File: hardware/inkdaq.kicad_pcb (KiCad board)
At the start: 2 copper layers, 6 x 23.2 mm, 3 parts, among them U1 INA333xxDRG

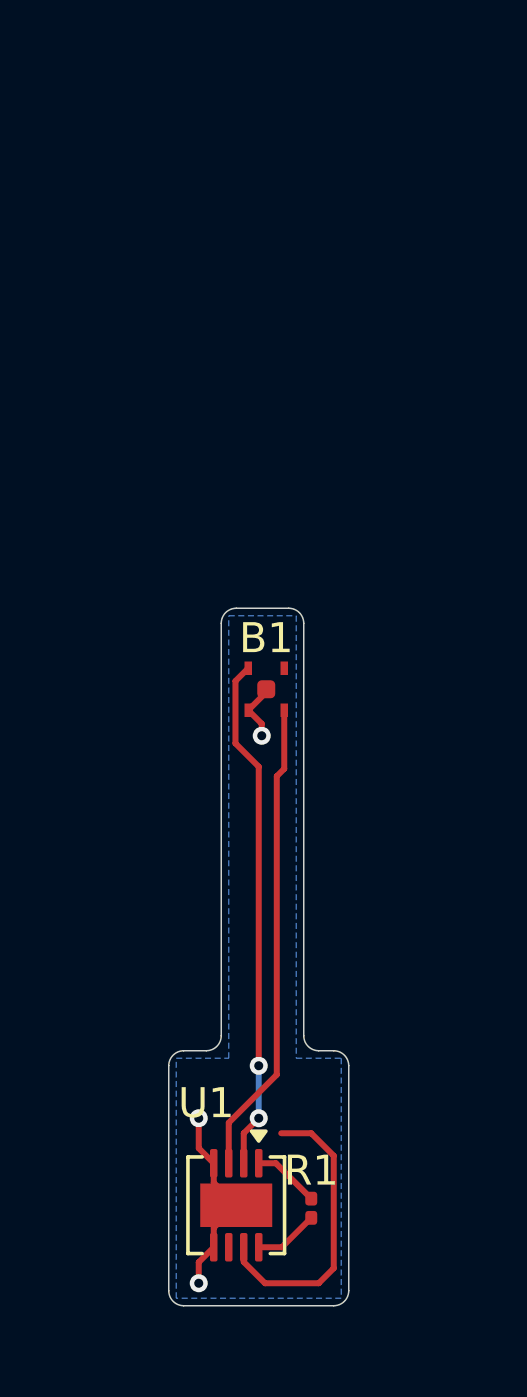
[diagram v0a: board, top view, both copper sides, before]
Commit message: add LCSC part numbers
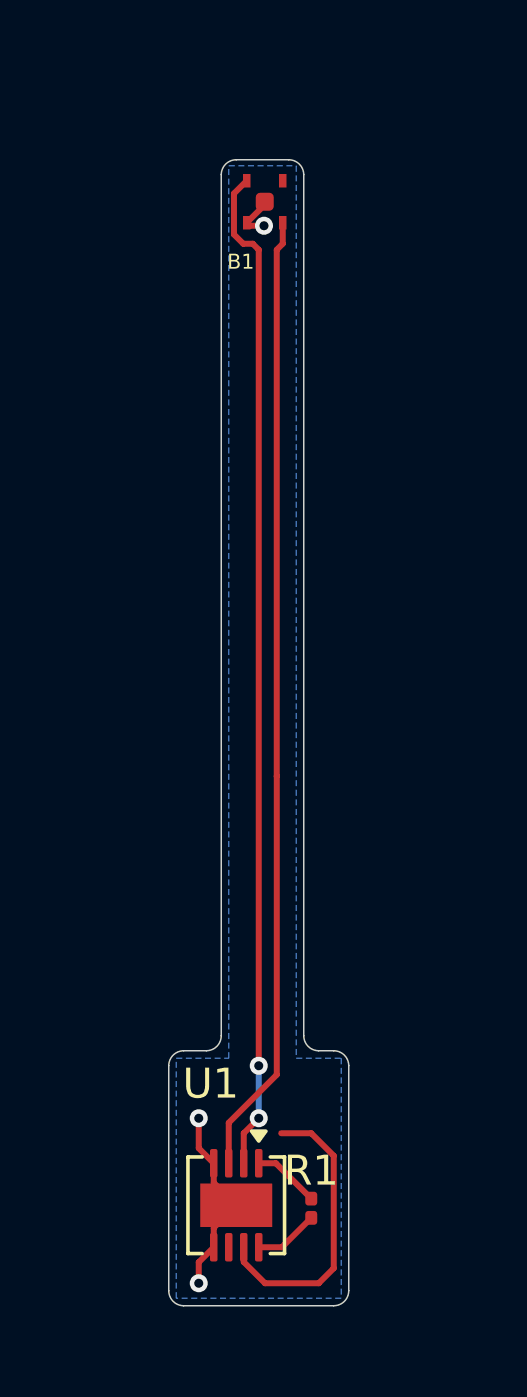
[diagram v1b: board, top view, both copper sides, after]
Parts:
- moved B1 16.3 mm to (157.2, 87.0)
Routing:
- net HSFPAR_V_NEG: track 17.2 -> 33.7 mm
- net HSFPAR_V_POS: track 15.9 -> 32.1 mm
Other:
- board size 6 x 23.2 mm -> 6 x 38.2 mm
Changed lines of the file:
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@@
+			)
+		)
+		(property "LCSC" "C851698"
+			(at 0 0 270)
+			(unlocked yes)
+			(layer "F.Fab")
+			(hide yes)
+			(effects
+				(font
+					(size 1 1)
+					(thickness 0.15)
+				)
 			)
 		)
@@
 	(footprint "inkdaq_footprints:HSFPAR004A"
 		(layer "F.Cu")
-		(at 157.25 103.2)
+		(at 157.2 86.95)
 		(descr "ALPSALPINE HSFPAR Series High-sensitivity Force Sensor")
 		(property "Reference" "B1"
-			(at 0 -4.45 0)
+			(at -0.8 -0.75 0)
 			(unlocked yes)
 			(layer "F.SilkS")
 			(effects
 				(font
-					(size 1 1)
-					(thickness 0.1)
+					(size 0.5 0.5)
+					(thickness 0.05)
 				)
 			)
@@
 		)
 		(property "Description" "ALPSALPINE HSFPAR Series High-sensitivity Force Sensor"
+			(at 0 0 0)
+			(unlocked yes)
+			(layer "F.Fab")
+			(hide yes)
+			(effects
+				(font
+					(size 1 1)
+					(thickness 0.15)
+				)
+			)
+		)
+		(property "LCSC" "C470800"
 			(at 0 0 0)
 			(unlocked yes)
@@
 		(tags "WSON NoLead")
 		(property "Reference" "U1"
-			(at -3.4 1 180)
+			(at -4.05 0.85 180)
 			(layer "F.SilkS")
 			(effects
@@
 				(font
 					(size 1.27 1.27)
+					(thickness 0.15)
+				)
+			)
+		)
+		(property "LCSC" "C2057429"
+			(at 0 0 270)
+			(unlocked yes)
+			(layer "F.Fab")
+			(hide yes)
+			(effects
+				(font
+					(size 1 1)
 					(thickness 0.15)
 				)
@@
 	)
 	(gr_arc
-		(start 158 97.75)
-		(mid 158.353553 97.896447)
-		(end 158.5 98.25)
+		(start 158 82.8)
+		(mid 158.353553 82.946447)
+		(end 158.5 83.3)
 		(stroke
 			(width 0.05)
@@
 	)
 	(gr_line
-		(start 158.5 98.25)
+		(start 158.5 83.3)
 		(end 158.5 112)
 		(stroke
@@
 	(gr_line
 		(start 155.75 112)
-		(end 155.75 98.25)
+		(end 155.75 83.3)
 		(stroke
 			(width 0.05)
@@
 	)
 	(gr_arc
-		(start 155.75 98.25)
-		(mid 155.896447 97.896447)
-		(end 156.25 97.75)
+		(start 155.75 83.3)
+		(mid 155.896447 82.946447)
+		(end 156.25 82.8)
 		(stroke
 			(width 0.05)
@@
 	)
 	(gr_line
-		(start 156.25 97.75)
-		(end 158 97.75)
+		(start 156.25 82.8)
+		(end 158 82.8)
 		(stroke
 			(width 0.05)
@@
 	)
 	(segment
+		(start 156.7 85)
+		(end 156.6 84.9)
+		(width 0.2)
+		(layer "F.Cu")
+		(net 3)
+	)
+	(segment
 		(start 155.5 119.05)
 		(end 155.5 118.4)
@@
 	)
 	(segment
-		(start 157.25 100.45)
-		(end 157.25 100.55)
+		(start 157.2 84.2)
+		(end 157.2 84.3)
 		(width 0.2)
 		(layer "F.Cu")
@@
 	)
 	(segment
-		(start 157.25 100.55)
-		(end 156.65 101.15)
+		(start 157.174998 85)
+		(end 156.7 85)
+		(width 0.2)
+		(layer "F.Cu")
+		(net 3)
+	)
+	(segment
+		(start 157.2 84.3)
+		(end 156.6 84.9)
 		(width 0.2)
 		(layer "F.Cu")
@@
 	)
 	(segment
-		(start 157.1 102)
-		(end 157.1 101.6)
-		(width 0.2)
-		(layer "F.Cu")
-		(net 3)
-	)
-	(segment
 		(start 155 115.75)
 		(end 155.5 116.25)
-		(width 0.2)
-		(layer "F.Cu")
-		(net 3)
-	)
-	(segment
-		(start 157.1 101.6)
-		(end 156.65 101.15)
 		(width 0.2)
 		(layer "F.Cu")
@@
 	)
 	(via
-		(at 157.1 102)
+		(at 157.174998 85)
 		(size 0.6)
 		(drill 0.3)
@@
 	)
 	(segment
+		(start 156 114.900057)
+		(end 157.601 113.299057)
+		(width 0.2)
+		(layer "F.Cu")
+		(net 5)
+	)
+	(segment
+		(start 157.8 85.6)
+		(end 157.8 84.9)
+		(width 0.2)
+		(layer "F.Cu")
+		(net 5)
+	)
+	(segment
+		(start 157.6 85.8)
+		(end 157.8 85.6)
+		(width 0.2)
+		(layer "F.Cu")
+		(net 5)
+	)
+	(segment
 		(start 157.601 113.299057)
 		(end 157.601 103.351)
@@
 	)
 	(segment
-		(start 157.85 103.102)
-		(end 157.601 103.351)
-		(width 0.2)
-		(layer "F.Cu")
-		(net 5)
-	)
-	(segment
 		(start 156 116.25)
 		(end 156 114.900057)
@@
 	)
 	(segment
-		(start 157.85 101.15)
-		(end 157.85 103.102)
+		(start 157.6 103.35)
+		(end 157.6 85.8)
 		(width 0.2)
 		(layer "F.Cu")
@@
 	)
 	(segment
-		(start 156 114.900057)
-		(end 157.601 113.299057)
+		(start 157.601 103.351)
+		(end 157.6 103.35)
 		(width 0.2)
 		(layer "F.Cu")
@@
 	)
 	(segment
-		(start 157 103.031374)
-		(end 156.224 102.255374)
+		(start 156.174 83.926)
+		(end 156.6 83.5)
+		(width 0.2)
+		(layer "F.Cu")
+		(net 7)
+	)
+	(segment
+		(start 157 85.8)
+		(end 156.8 85.6)
+		(width 0.2)
+		(layer "F.Cu")
+		(net 7)
+	)
+	(segment
+		(start 156.484313 85.6)
+		(end 156.174 85.289687)
+		(width 0.2)
+		(layer "F.Cu")
+		(net 7)
+	)
+	(segment
+		(start 156.174 85.289687)
+		(end 156.174 83.926)
+		(width 0.2)
+		(layer "F.Cu")
+		(net 7)
+	)
+	(segment
+		(start 156.8 85.6)
+		(end 156.484313 85.6)
 		(width 0.2)
 		(layer "F.Cu")
@@
 	)
 	(segment
-		(start 156.224 102.255374)
-		(end 156.224 100.176)
-		(width 0.2)
-		(layer "F.Cu")
-		(net 7)
-	)
-	(segment
 		(start 157 113)
-		(end 157 103.031374)
-		(width 0.2)
-		(layer "F.Cu")
-		(net 7)
-	)
-	(segment
-		(start 156.224 100.176)
-		(end 156.65 99.75)
+		(end 157 85.8)
 		(width 0.2)
 		(layer "F.Cu")
@@
 		(polygon
 			(pts
-				(xy 156 98) (xy 158.25 98) (xy 158.25 112.75) (xy 159.75 112.75) (xy 159.75 120.75) (xy 154.25 120.75)
+				(xy 156 83) (xy 158.25 83) (xy 158.25 112.75) (xy 159.75 112.75) (xy 159.75 120.75) (xy 154.25 120.75)
 				(xy 154.25 112.75) (xy 156 112.75)
 			)

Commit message: my awful attempt at making a breakaway pcb in a larger panel since JLC doesnt like it being so small
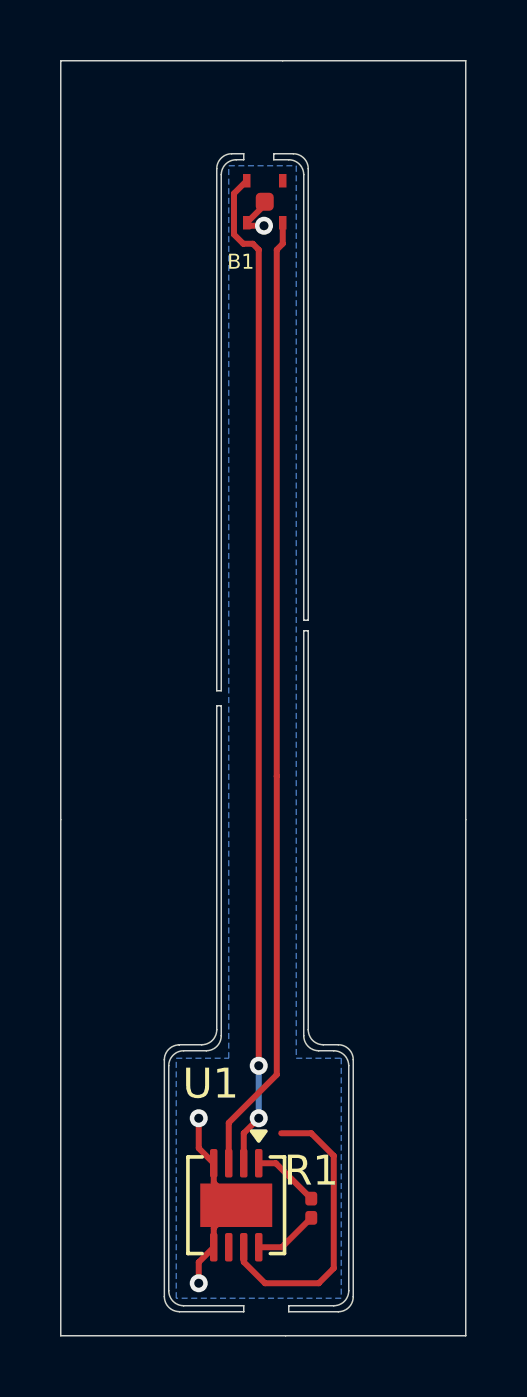
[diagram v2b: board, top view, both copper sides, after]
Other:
- board size 6 x 38.2 mm -> 13.5 x 42.5 mm
